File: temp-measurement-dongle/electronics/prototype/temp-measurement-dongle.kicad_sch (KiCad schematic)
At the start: 76 parts, among them J1 USB2UART, J2 1.47 IPS LCD, J3 ConnBattery, J4 RTD_PT100, Q1 SS8050, Q2 SS8050, Q3 SS8050, SW1 RST, SW2 IN1, SW3 Boot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

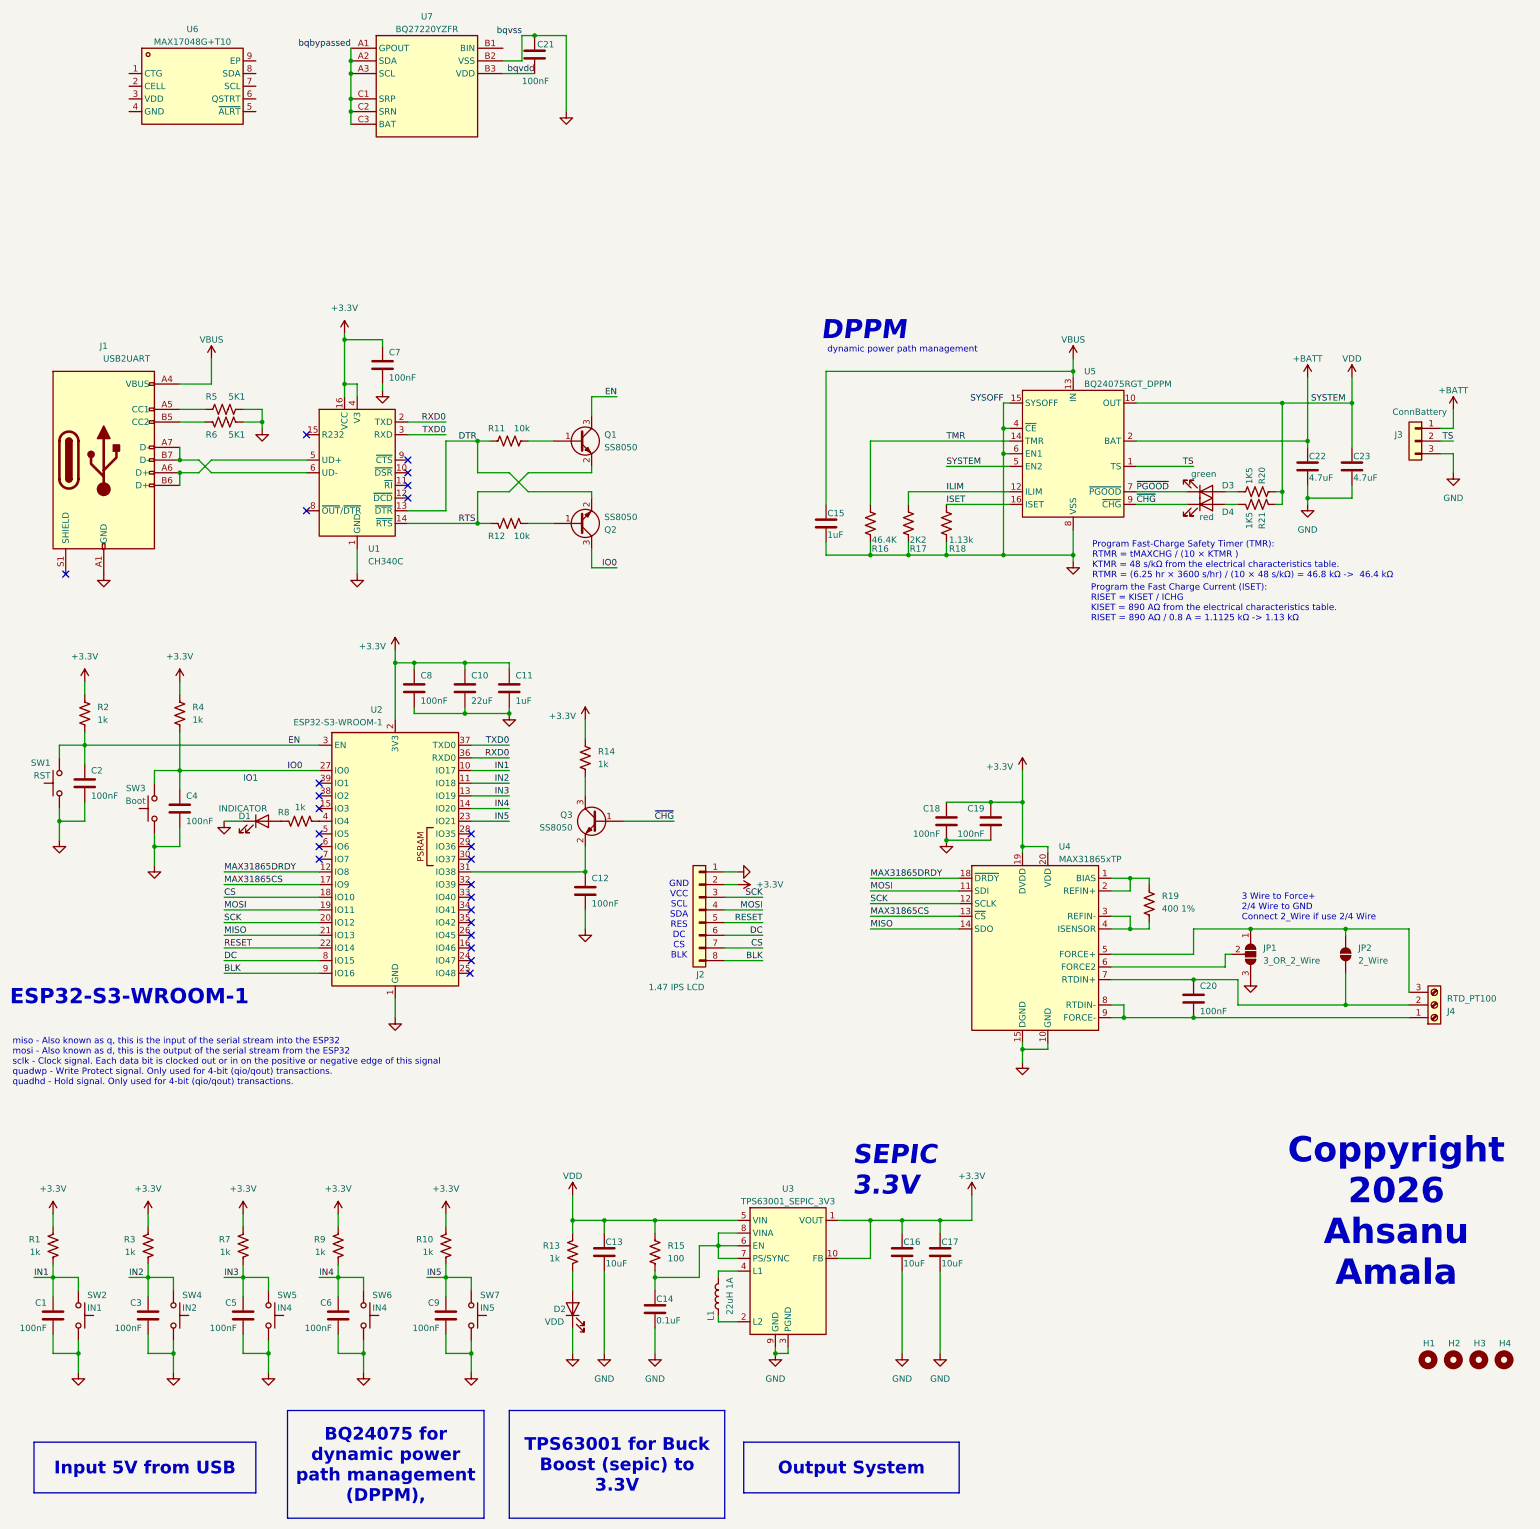
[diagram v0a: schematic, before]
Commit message: feat(tmd): update schematic to use fuel gauge bq27421
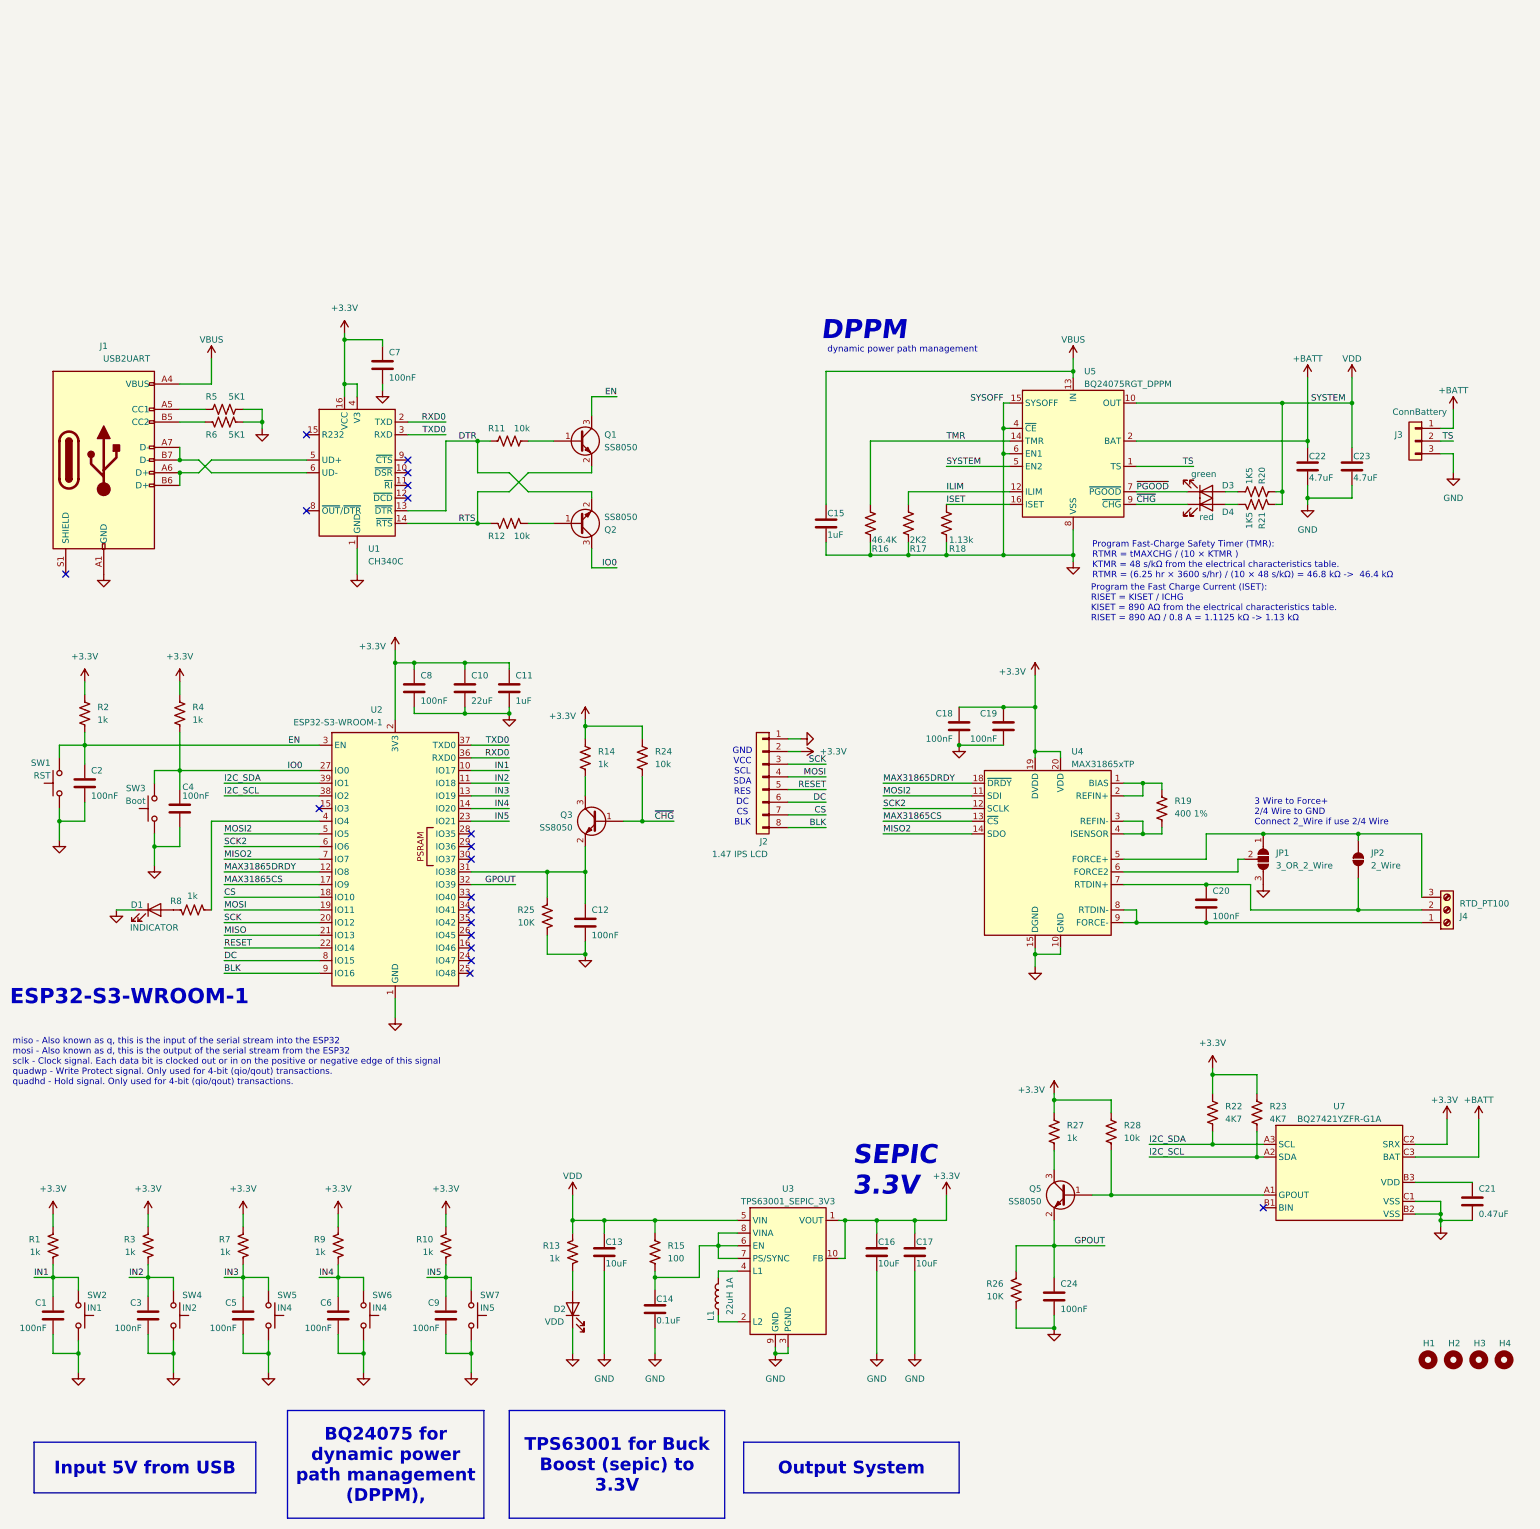
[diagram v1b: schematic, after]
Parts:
- removed U6: MAX17048G+T10, easyeda2kicad:TDFN-8_L2.0-W2.0-P0.50-BL-EP1.2, symbol easyeda2kicad:MAX17048G+T10
- removed U7: BQ27220YZFR, easyeda2kicad:DSBGA-9_L1.7-W1.6-R3-C3-P0.50-BL, symbol easyeda2kicad:BQ27220YZFR
- added C24: 100nF, Capacitor_SMD:C_0805_2012Metric_Pad1.18x1.45mm_HandSolder, symbol Device:C
- added Q5: SS8050, Package_TO_SOT_SMD:SOT-23_Handsoldering, symbol Transistor_BJT:BC817
- added R22, R23: 4K7, Resistor_SMD:R_0805_2012Metric_Pad1.20x1.40mm_HandSolder, symbol Device:R_US
- added R24, R28: 10k, Resistor_SMD:R_0805_2012Metric_Pad1.20x1.40mm_HandSolder, symbol Device:R_US
- added R25, R26: 10K, Resistor_SMD:R_0805_2012Metric_Pad1.20x1.40mm_HandSolder, symbol Device:R_US
- added R27: 1k, Resistor_SMD:R_0805_2012Metric_Pad1.20x1.40mm_HandSolder, symbol Device:R_US
- added U7: BQ27421YZFR-G1A, easyeda2kicad:DSBGA-9_L1.5-W1.5-R3-C3-P0.50-BL, symbol easyeda2kicad:BQ27421YZFR-G1A
- C21: value 100nF -> 0.47uF
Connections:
- net bqvdd is gone; now on net GND: C21.2
- net +3.3V: now also R22.1, R23.1, R24.1, R27.1, R28.1, U7.C2 (SRX)
- net +BATT: now also U7.C3 (BAT)
- net GND: now also C24.2, R25.2, R26.2, U7.B2 (VSS), U7.C1 (VSS); no longer C21.1
- net MISO: no longer U4.14 (SDO)
- net MOSI: no longer U4.11 (SDI)
- net SCK: no longer U4.12 (SCLK)
- net ~{CHG}: now also R24.2
- net at C12.1, Q3.2 (E), U2.31 (IO38): now also R25.1
- net GPOUT: now reaches U2.32 (IO39)
- net GPOUT: now also C24.1, Q5.2 (E), R26.1
- net I2C_SCL: now reaches U2.38 (IO2)
- net I2C_SCL: now also R23.2, U7.A2 (SDA)
- net I2C_SDA: now reaches U2.39 (IO1)
- net I2C_SDA: now also R22.2, U7.A3 (SCL)
- net MOSI2: now reaches U2.5 (IO5)
- net MOSI2: now also U4.11 (SDI)
- net SCK2: now reaches U2.6 (IO6)
- net SCK2: now also U4.12 (SCLK)
- net MISO2: now reaches U2.7 (IO7)
- net MISO2: now also U4.14 (SDO)
- new net: Q5.1 (B), R28.2, U7.A1 (GPOUT)
- new net: Q5.3 (C), R27.2
- new net: C21.1, U7.B3 (VDD)
- no-connect marks 24 -> 19
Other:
- moved on the sheet: C12, C16, C17, C18, C19, C20, J2, J4, JP1, JP2, R19, U4

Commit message: chore: move libraries to mkl
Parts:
- R19: value 400 1% -> 430 1%
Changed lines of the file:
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@@
 			)
 		)
-		(property "Value" "400 1%"
+		(property "Value" "430 1%"
 			(at 248.92 122.936 0)
 			(show_name no)
@@
 			(at 246.38 121.92 0)
 			(hide yes)
+			(show_name no)
+			(do_not_autoplace no)
+			(effects
+				(font
+					(size 1.27 1.27)
+				)
+			)
+		)
+		(property "Field5" ""
+			(at 246.38 121.92 0)
+			(hide yes)

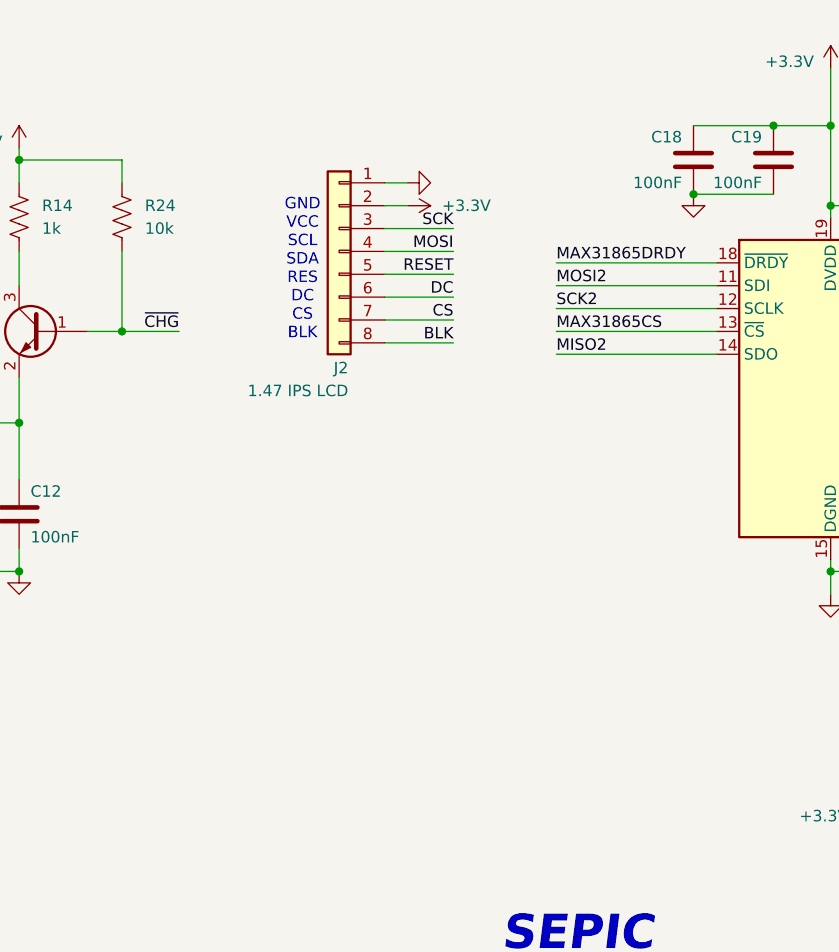
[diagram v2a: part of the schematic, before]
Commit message: feat(tmd): add lcd jumper
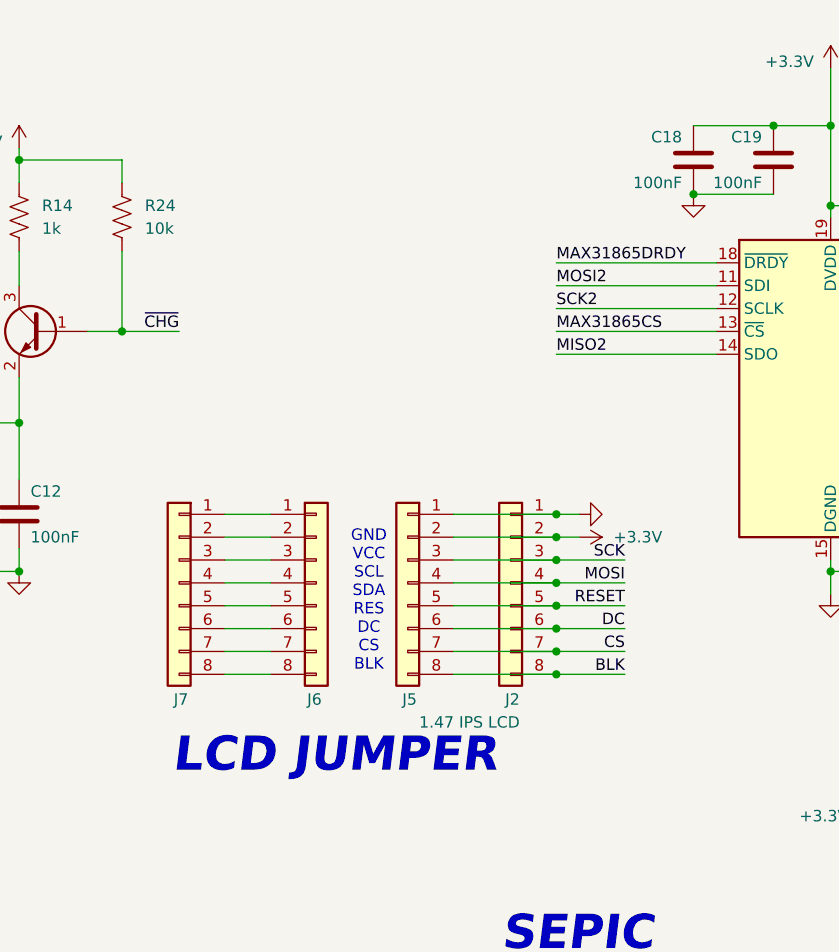
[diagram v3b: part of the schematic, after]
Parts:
- added J5, J6, J7: lcd jumper, Connector_PinHeader_2.54mm:PinHeader_1x08_P2.54mm_Vertical, symbol Connector_Generic:Conn_01x08
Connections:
- net +3.3V: now also J5.2 (Pin_2)
- net BLK: now also J5.8 (Pin_8)
- net CS: now also J5.7 (Pin_7)
- net DC: now also J5.6 (Pin_6)
- net GND: now also J5.1 (Pin_1)
- net MOSI: now also J5.4 (Pin_4)
- net RESET: now also J5.5 (Pin_5)
- net SCK: now also J5.3 (Pin_3)
- new net: J6.1 (Pin_1), J7.1 (Pin_1)
- new net: J6.2 (Pin_2), J7.2 (Pin_2)
- new net: J6.3 (Pin_3), J7.3 (Pin_3)
- new net: J6.4 (Pin_4), J7.4 (Pin_4)
- new net: J6.5 (Pin_5), J7.5 (Pin_5)
- new net: J6.6 (Pin_6), J7.6 (Pin_6)
- new net: J6.7 (Pin_7), J7.7 (Pin_7)
- new net: J6.8 (Pin_8), J7.8 (Pin_8)
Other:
- note added: "LCD JUMPER"
- moved on the sheet: J2
